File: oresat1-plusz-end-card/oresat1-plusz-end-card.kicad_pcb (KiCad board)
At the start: 4 copper layers, 99.8 x 94.6 mm, 99 parts, among them J1 J-SAMTEC-TFM-120-01-L-D-RA, J2 M55-7101242R, J3 M55-7101242R, J4 M55-7101242R, J5 M55-7101242R, J6 U.FL-R-SMT-1, Q1 DMP2240UDM, Q11 DMP2240UDM-7, Q2 PMV45EN, Q3 PMV45EN, Q4 PMV45EN, Q6 PMV45EN, Q9 DMP2240UDM-7, U11 MIC842LYC5, U12 MIC842LYC5, U2 MAX7310, U201 TS5A21366, U202 TS5A21366, U203 TS5A21366, U204 TS5A21366

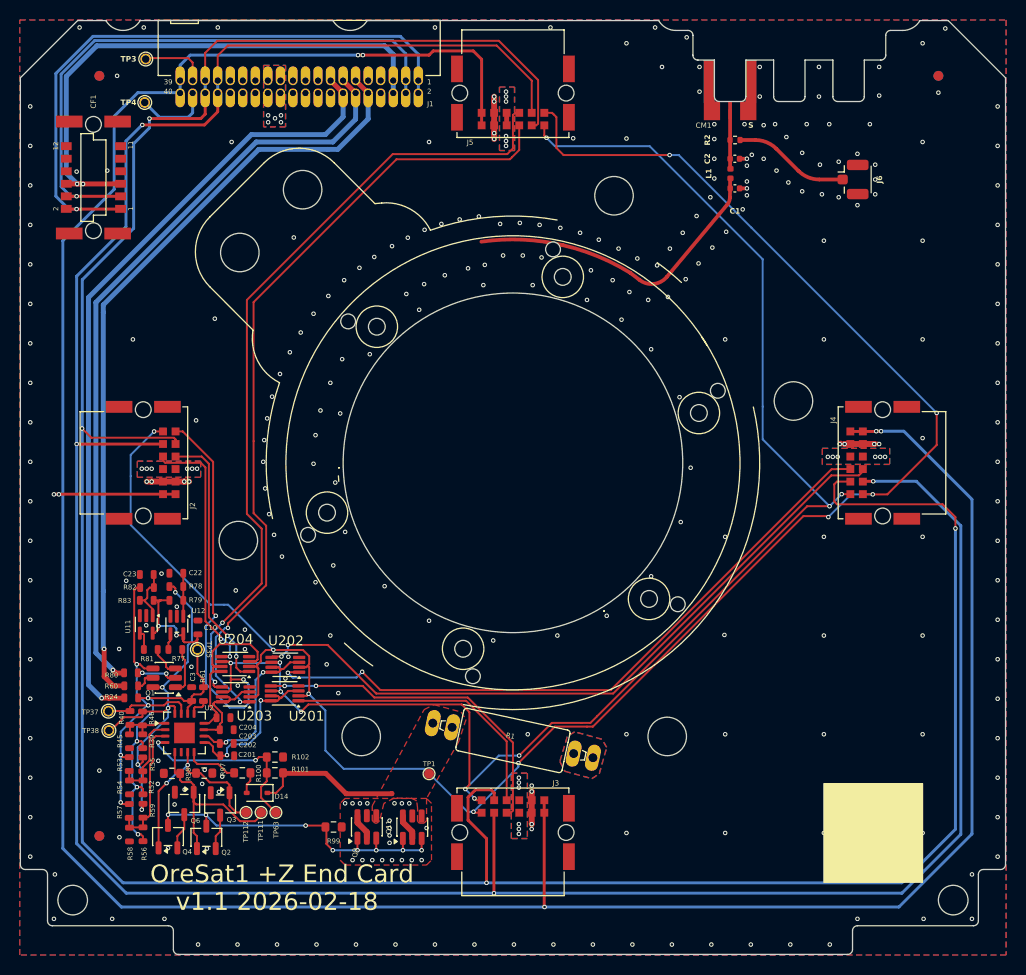
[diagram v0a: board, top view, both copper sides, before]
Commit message: Fixed weird footprint sync error that kept popping up on DRC around the mounting holes because of the polygon zone keepout areas. Also found a huge mistake in the schematic, fixed, still needs to be routed.
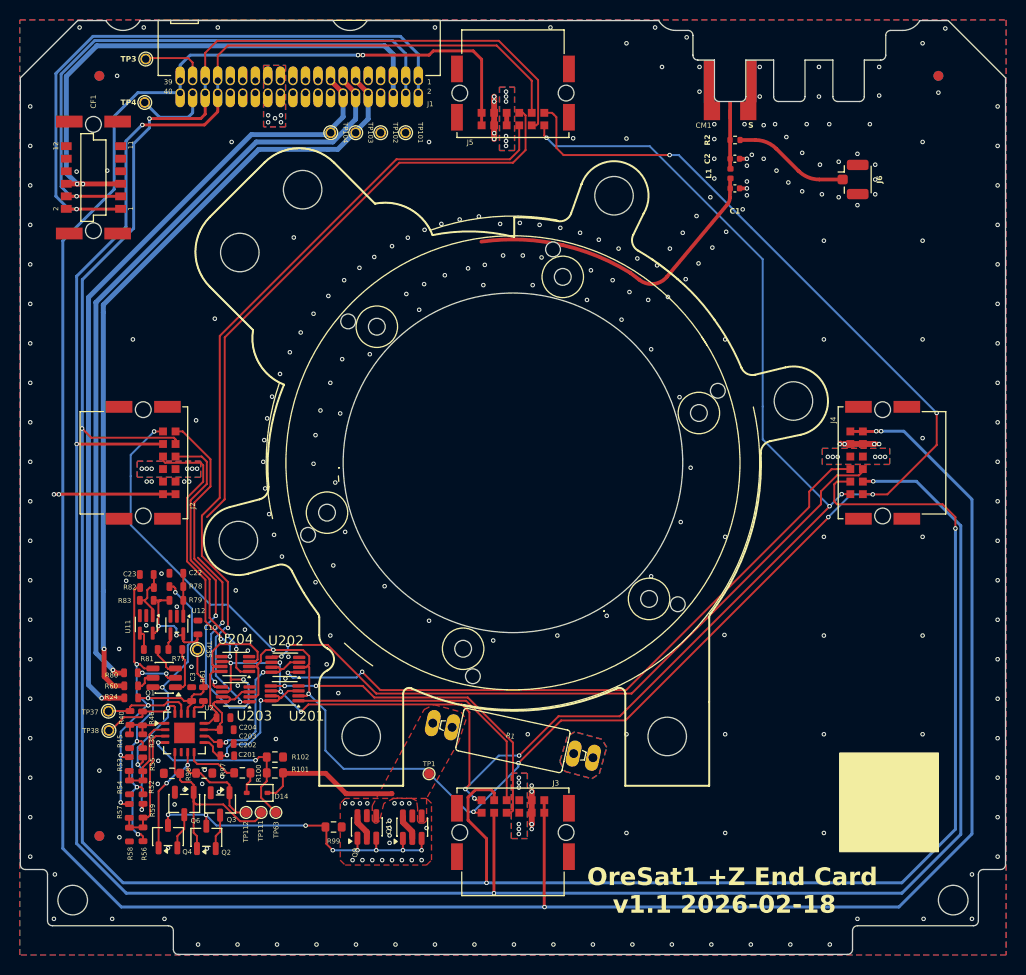
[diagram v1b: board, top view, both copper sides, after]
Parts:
- added TP101: TestPoint-MinTH, oresat-misc:TestPoint-0.75mm-th, F.Cu at (137.6, 69.1)
- added TP102: TestPoint-MinTH, oresat-misc:TestPoint-0.75mm-th, F.Cu at (135.1, 69.1)
- added TP103: TestPoint-MinTH, oresat-misc:TestPoint-0.75mm-th, F.Cu at (132.6, 69.1)
- added TP104: TestPoint-MinTH, oresat-misc:TestPoint-0.75mm-th, F.Cu at (130.0, 69.1)
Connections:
- J1 pad 10: /OPD_SDA -> Net-(J1-Pad10)
- J1 pad 12: /OPD_SCL -> /OPD_SDA
- J1 pad 14: /OPD_PWR -> /OPD_SCL
- J1 pad 16: unconnected-(J1-Pad16) -> /OPD_PWR
- J1 pad 7: unconnected-(J1-Pad7) -> Net-(J1-Pad7)
- J1 pad 8: unconnected-(J1-Pad8) -> Net-(J1-Pad8)
- J1 pad 9: unconnected-(J1-Pad9) -> Net-(J1-Pad9)
- J2 pad 10: /CAN1_L -> /CAN1_H
- J2 pad 11: /OPD/C3-UART-TX -> /CAN1_L
- J2 pad 12: /OPD/C3-UART-RX -> /CAN1_L
- J3 pad 10: /CAN1_L -> /CAN1_H
- J3 pad 11: /OPD/C3-UART-TX -> /CAN1_L
- J3 pad 12: /OPD/C3-UART-RX -> /CAN1_L
- J4 pad 10: /CAN1_L -> /CAN1_H
- J4 pad 11: /OPD/C3-UART-TX -> /CAN1_L
- J4 pad 12: /OPD/C3-UART-RX -> /CAN1_L
- J5 pad 10: /CAN1_L -> /CAN1_H
- J5 pad 11: /OPD/C3-UART-TX -> /CAN1_L
- J5 pad 12: /OPD/C3-UART-RX -> /CAN1_L
- R24 pad 1: /OPD_PWR -> /OPD/OPD_PWR
- R60 pad 1: /OPD_SDA -> /OPD/OPD_SDA
- R80 pad 1: /OPD_SCL -> /OPD/OPD_SCL
- U201 pad 2: /OPD/C3-UART-TX -> /C3_UART_TX
- U201 pad 6: /OPD/C3-UART-RX -> /C3_UART_RX
- U202 pad 2: /OPD/C3-UART-TX -> /C3_UART_TX
- U202 pad 6: /OPD/C3-UART-RX -> /C3_UART_RX
- U203 pad 2: /OPD/C3-UART-TX -> /C3_UART_TX
- U203 pad 6: /OPD/C3-UART-RX -> /C3_UART_RX
- U204 pad 2: /OPD/C3-UART-TX -> /C3_UART_TX
- U204 pad 6: /OPD/C3-UART-RX -> /C3_UART_RX
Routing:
- net (no net): track 0.00 -> 386.1 mm
- net /OPD/C3-UART-TX: track 194.4 -> 0.00 mm, vias 9 -> 0
- net /OPD/C3-UART-RX: track 190.3 -> 0.00 mm, vias 12 -> 0
- net GND: track 16.5 -> 12.2 mm, vias 275 -> 272
- net /OPD/MX-UART-TX: track 80.3 -> 77.1 mm
- net /OPD/MY-UART-RX: track 27.0 -> 28.3 mm
- net /OPD/MY-UART-TX: track 26.2 -> 27.5 mm
- net /OPD/MX-UART-RX: track 81.1 -> 82.2 mm
- net /OPD/PY-UART-RX: track 68.6 -> 69.5 mm
- net /OPD/PY-UART-TX: track 72.3 -> 73.1 mm
- net VBUS: vias 46 -> 49
- net /C3_UART_TX: vias 0 -> 9
- net /C3_UART_RX: vias 0 -> 12

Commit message: Fixed HW errors
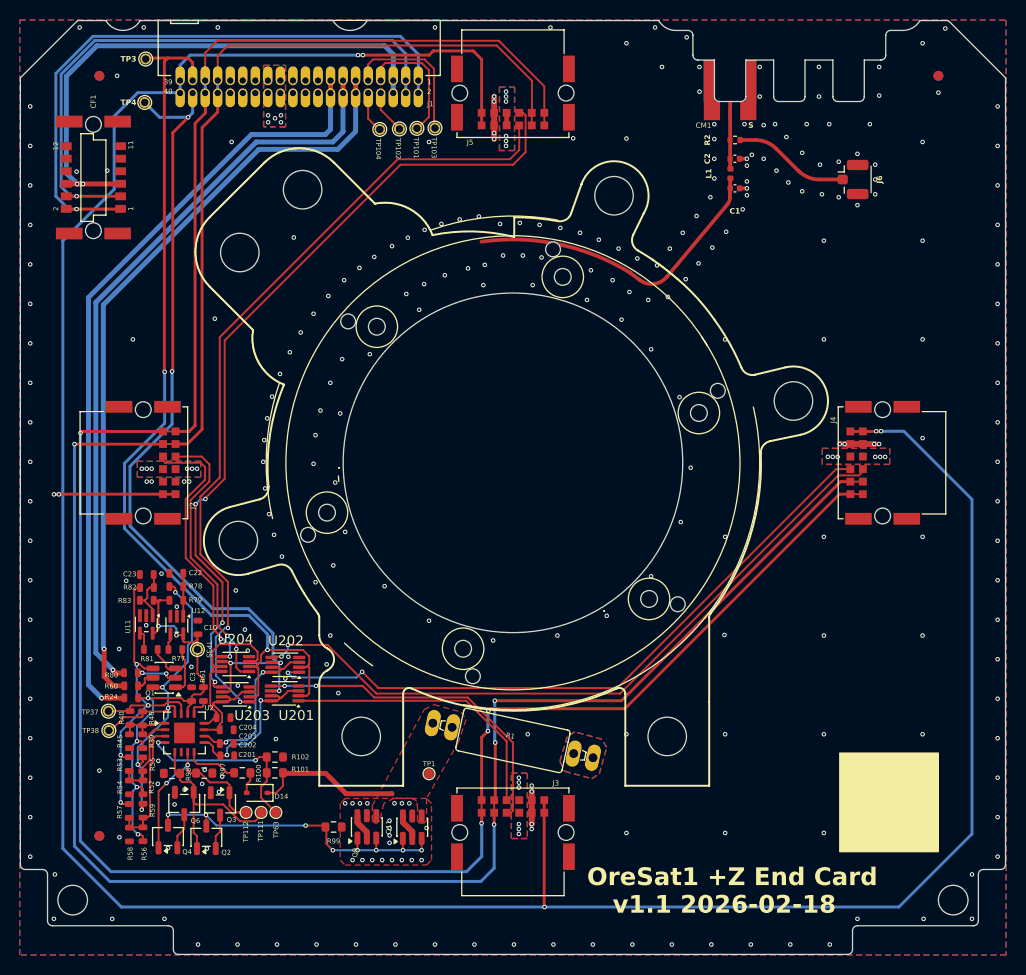
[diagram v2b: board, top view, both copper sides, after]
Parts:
- moved TP103 8.04 mm to (140.6, 68.6)
- moved TP104 4.98 mm to (135.0, 68.7)
- moved TP102 1.94 mm to (137.0, 68.7)
- moved TP101 1.23 mm to (138.8, 68.6)
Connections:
- R24 pad 1: /OPD/OPD_PWR -> /OPD_PWR
- R60 pad 1: /OPD/OPD_SDA -> /OPD_SDA
- R80 pad 1: /OPD/OPD_SCL -> /OPD_SCL
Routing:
- net (no net): track 386.1 -> 0.00 mm
- net /C3_UART_TX: track 6.80 -> 94.3 mm, vias 9 -> 2
- net /C3_UART_RX: track 7.67 -> 88.4 mm, vias 12 -> 5
- net /CAN1_L: track 293.3 -> 236.9 mm
- net /CAN1_H: track 280.5 -> 239.1 mm
- net Net-(J1-Pad9): track 0.00 -> 15.0 mm
- net Net-(J1-Pad7): track 0.00 -> 13.1 mm
- net /OPD/MX-UART-TX: track 77.1 -> 82.0 mm, vias 2 -> 4
- net Net-(J1-Pad8): track 0.00 -> 4.43 mm
- net Net-(J1-Pad10): track 0.00 -> 4.15 mm
- net /OPD/PY-UART-RX: track 69.5 -> 68.5 mm
- net /OPD_PWR: track 81.0 -> 80.0 mm
- net /OPD_SDA: track 79.2 -> 78.1 mm
- net /OPD_SCL: track 77.7 -> 76.6 mm
- net /OPD/PY-UART-TX: track 73.1 -> 72.3 mm
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
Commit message: added clearance around HW
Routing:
- net /OPD/PY-UART-RX: track 68.5 -> 69.6 mm
- net /CAN1_H: track 239.1 -> 238.5 mm
- net GND: vias 271 -> 269

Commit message: SBAND & HELICAL RF CHANGES
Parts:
- removed R2: NP, Resistor_SMD:R_0402_1005Metric
- added CM2: 2477330-1, oresat-connectors:J-MOLEX-SMPM-073300-002X, F.Cu at (176.4, 61.7)
- moved J6 1.63 mm to (181.4, 73.5)
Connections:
- net /S_BAND renamed Net-(C2-Pad2)
- net /S_BAND_FEED renamed /HELICAL
- J6 pad 1: /S_BAND_U_FL -> /PATCH
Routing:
- net /S_BAND_U_FL: track 11.8 -> 0.00 mm
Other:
- board text added: "U.FL"
